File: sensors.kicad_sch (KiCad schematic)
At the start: 19 parts, among them IC2 ASM330LHHTR, IC3 MAX-M10S-00B, J3 Conn_Coaxial, U4 LSM303C, U5 LPS22HH

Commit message: Added all sensors and telemetry modem
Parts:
- FB2: footprint Capacitor_SMD:C_0201_0603Metric -> Capacitor_SMD:C_0603_1608Metric
- R2: footprint Resistor_SMD:R_0201_0603Metric -> Resistor_SMD:R_0402_1005Metric
- R3: footprint (none) -> Resistor_SMD:R_0402_1005Metric
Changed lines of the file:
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@@
 			)
 		)
-		(property "Footprint" "Resistor_SMD:R_0201_0603Metric"
+		(property "Footprint" "Resistor_SMD:R_0402_1005Metric"
 			(at 98.552 44.45 90)
 			(effects
@@
 			)
 		)
-		(property "Footprint" "Capacitor_SMD:C_0201_0603Metric"
+		(property "Footprint" "Capacitor_SMD:C_0603_1608Metric"
 			(at 156.972 115.57 90)
 			(effects
@@
 			)
 		)
-		(property "Footprint" ""
+		(property "Footprint" "Resistor_SMD:R_0402_1005Metric"
 			(at 106.172 44.45 90)
 			(effects

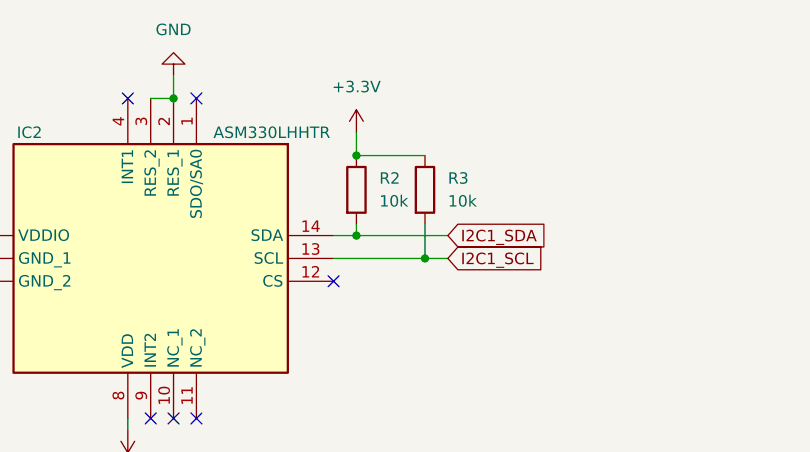
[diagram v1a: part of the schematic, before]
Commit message: Added IO
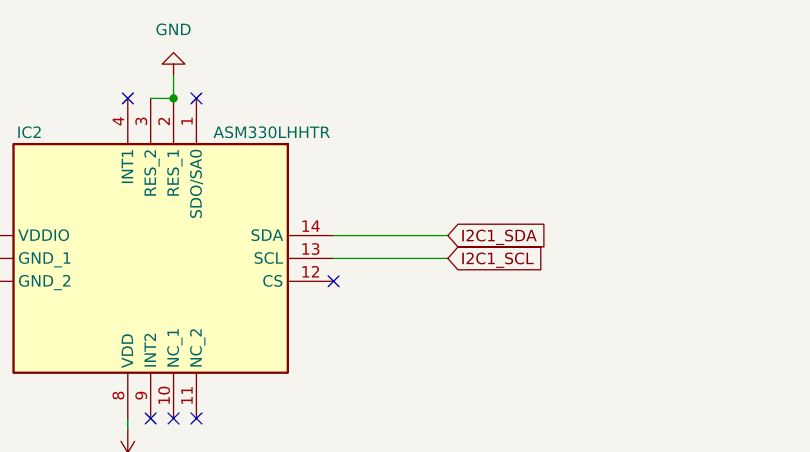
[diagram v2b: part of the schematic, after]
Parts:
- removed R2, R3: 10k, Resistor_SMD:R_0402_1005Metric, symbol Device:R

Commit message: Change 0201 to 0403
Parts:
- C20, C21, C22, C23, C24, C25, C26, C27: footprint Capacitor_SMD:C_0201_0603Metric -> Capacitor_SMD:C_0402_1005Metric
- C29: footprint Capacitor_SMD:C_0603_1608Metric -> Capacitor_SMD:C_0402_1005Metric
- R7: footprint Resistor_SMD:R_0201_0603Metric -> Capacitor_SMD:C_0402_1005Metric
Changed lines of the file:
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@@
 			)
 		)
-		(property "Footprint" "Capacitor_SMD:C_0201_0603Metric"
+		(property "Footprint" "Capacitor_SMD:C_0402_1005Metric"
 			(at 33.9852 57.15 0)
 			(effects
@@
 			)
 		)
-		(property "Footprint" "Capacitor_SMD:C_0201_0603Metric"
+		(property "Footprint" "Capacitor_SMD:C_0402_1005Metric"
 			(at 20.0152 57.15 0)
 			(effects
@@
 			)
 		)
-		(property "Footprint" "Capacitor_SMD:C_0201_0603Metric"
+		(property "Footprint" "Capacitor_SMD:C_0402_1005Metric"
 			(at 243.5352 45.72 0)
 			(effects
@@
 			)
 		)
-		(property "Footprint" "Capacitor_SMD:C_0603_1608Metric"
+		(property "Footprint" "Capacitor_SMD:C_0402_1005Metric"
 			(at 159.7152 133.35 0)
 			(effects
@@
 			)
 		)
-		(property "Footprint" "Capacitor_SMD:C_0201_0603Metric"
+		(property "Footprint" "Capacitor_SMD:C_0402_1005Metric"
 			(at 46.6852 57.15 0)
 			(effects
@@
 			)
 		)
-		(property "Footprint" "Resistor_SMD:R_0201_0603Metric"
+		(property "Footprint" "Capacitor_SMD:C_0402_1005Metric"
 			(at 179.07 121.158 90)
 			(effects
@@
 			)
 		)
-		(property "Footprint" "Capacitor_SMD:C_0201_0603Metric"
+		(property "Footprint" "Capacitor_SMD:C_0402_1005Metric"
 			(at 230.8352 45.72 0)
 			(effects
@@
 			)
 		)
-		(property "Footprint" "Capacitor_SMD:C_0201_0603Metric"
+		(property "Footprint" "Capacitor_SMD:C_0402_1005Metric"
 			(at 26.3652 113.03 0)
 			(effects
@@
 			)
 		)
-		(property "Footprint" "Capacitor_SMD:C_0201_0603Metric"
+		(property "Footprint" "Capacitor_SMD:C_0402_1005Metric"
 			(at 221.9452 66.04 0)
 			(effects
@@
 			)
 		)
-		(property "Footprint" "Capacitor_SMD:C_0201_0603Metric"
+		(property "Footprint" "Capacitor_SMD:C_0402_1005Metric"
 			(at 218.1352 45.72 0)
 			(effects

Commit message: Added STM32_MX Project, LED, Fixed DRC Violations
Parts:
- D2: footprint DIONC1005X43N -> VanguardLib:DIONC1005X43N
- IC2: footprint LSM6DS3USTR -> VanguardLib:LSM6DS3USTR
- IC3: footprint MAXM10S00B -> VanguardLib:MAXM10S00B
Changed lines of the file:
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@@
 			)
 		)
-		(property "Footprint" "LSM6DS3USTR"
+		(property "Footprint" "VanguardLib:LSM6DS3USTR"
 			(at -4.75 66.04 0)
 			(effects
@@
 			)
 		)
-		(property "Footprint" "MAXM10S00B"
+		(property "Footprint" "VanguardLib:MAXM10S00B"
 			(at 226.06 204.14 0)
 			(effects
@@
 			)
 		)
-		(property "Footprint" "DIONC1005X43N"
+		(property "Footprint" "VanguardLib:DIONC1005X43N"
 			(at 229.54 120.65 0)
 			(effects
